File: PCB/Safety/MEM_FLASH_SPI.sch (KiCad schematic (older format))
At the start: 3 parts, among them U5 S70FL01GS

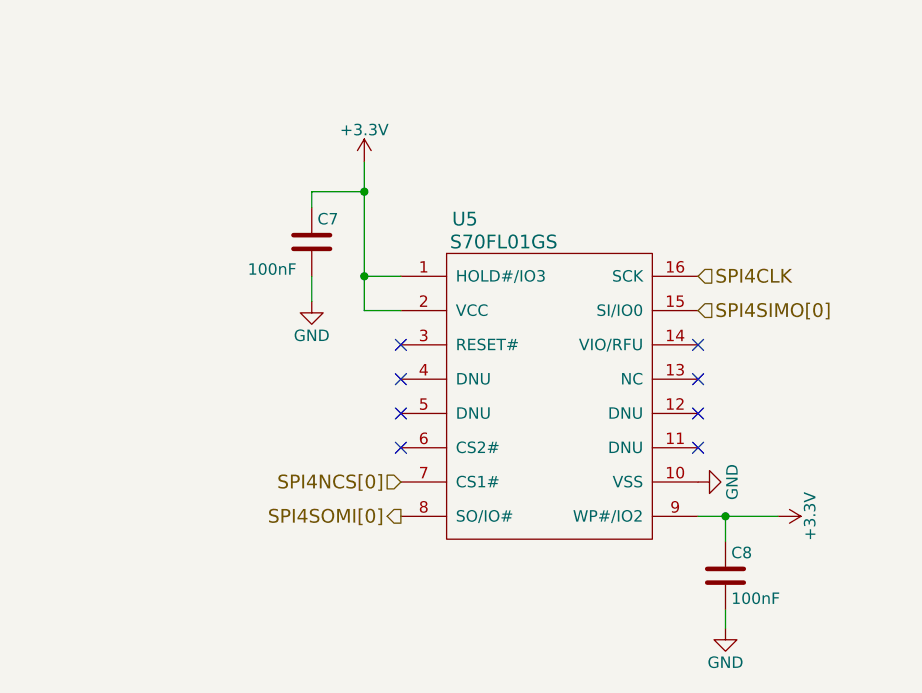
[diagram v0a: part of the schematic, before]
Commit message: New version (-4) from Fusari,s Drive.
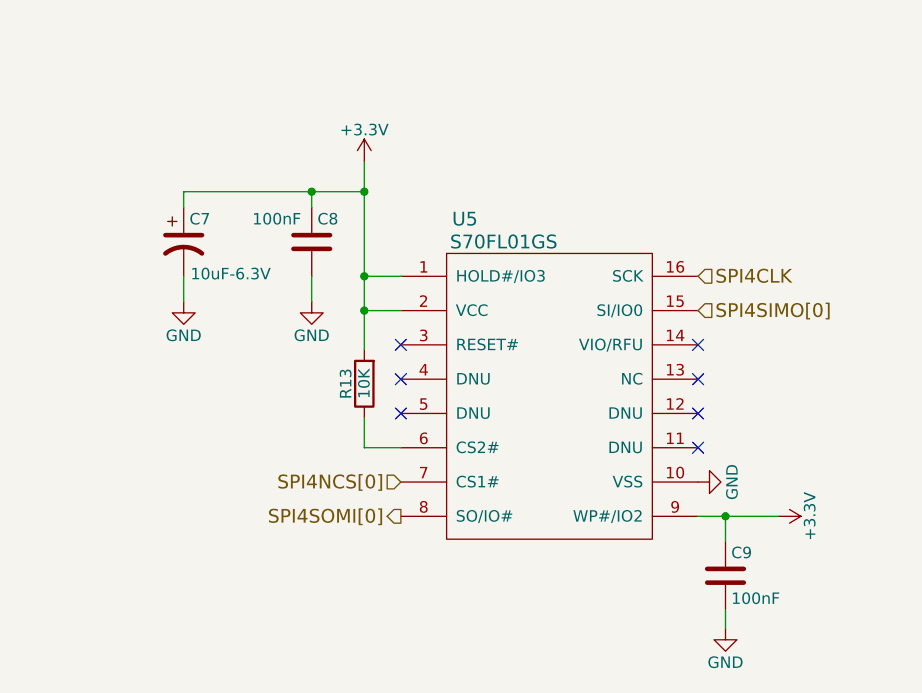
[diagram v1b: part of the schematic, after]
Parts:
- added C7: 10uF-6.3V, w_smd_cap:c_tant_A, symbol CP1
- added R13: 10K, w_smd_resistors:r_0603, symbol R
- C8: renamed from C7; Digikey (none) -> 478-5266-1-ND
- C9: renamed from C8; Digikey (none) -> 478-5266-1-ND
- U5: Digikey (none) -> 428-4016-1-ND
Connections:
- net +3V3: now also C7.1, R13.2
- net GND: now also C7.2
- net at U5.6 (CS2#): now also R13.1
- no-connect marks 8 -> 7
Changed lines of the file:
@@
 EESchema Schematic File Version 2
+LIBS:74xgxx
+LIBS:74xx
+LIBS:ac-dc
+LIBS:actel
+LIBS:adc-dac
+LIBS:Altera
+LIBS:analog_devices
+LIBS:analog_switches
+LIBS:atmel
+LIBS:audio
+LIBS:brooktre
+LIBS:cmos_ieee
+LIBS:cmos4000
+LIBS:conn
+LIBS:contrib
+LIBS:cypress
+LIBS:dc-dc
+LIBS:device
+LIBS:digital-audio
+LIBS:diode
+LIBS:display
+LIBS:dsp
+LIBS:elec-unifil
+LIBS:ESD_Protection
+LIBS:ftdi
+LIBS:gennum
+LIBS:graphic
+LIBS:hc11
+LIBS:intel
+LIBS:interface
+LIBS:ir
+LIBS:Lattice
+LIBS:linear
+LIBS:logo
+LIBS:maxim
+LIBS:memory
+LIBS:microchip
+LIBS:microchip_dspic33dsc
+LIBS:microchip_pic10mcu
+LIBS:microchip_pic12mcu
+LIBS:microchip_pic16mcu
+LIBS:microchip_pic18mcu
+LIBS:microchip_pic32mcu
+LIBS:microcontrollers
+LIBS:motor_drivers
+LIBS:motorola
+LIBS:msp430
+LIBS:nordicsemi
+LIBS:nxp_armmcu
+LIBS:onsemi
+LIBS:opto
+LIBS:Oscillators
+LIBS:philips
 LIBS:power
+LIBS:Power_Management
+LIBS:powerint
+LIBS:pspice
+LIBS:references
+LIBS:regul
+LIBS:relays
+LIBS:rfcom
+LIBS:sensors
+LIBS:silabs
+LIBS:siliconi
+LIBS:stm8
+LIBS:stm32
+LIBS:supertex
+LIBS:switches
+LIBS:texas
+LIBS:transf
+LIBS:transistors
+LIBS:ttl_ieee
+LIBS:valves
+LIBS:video
+LIBS:Xicor
+LIBS:xilinx
+LIBS:Zilog
 LIBS:CIAA_Safety_VTI_1.0-cache
 EELAYER 25 0
@@
 $Descr A4 11693 8268
 encoding utf-8
-Sheet 3 5
-Title "MEMORIA FLASH"
-Date "2016-06-02"
+Sheet 3 8
+Title "MODULO PROCESADOR SAFETY"
+Date "2016-09-01"
 Rev "1.0"
 Comp "PROYECTO CIAA SAFETY"
-Comment1 "Ing. Fusari Diego"
-Comment2 "MODULO PROCESADOR SAFETY"
-Comment3 "Licencia: Ver 'doc/LICENCIA.txt'"
+Comment1 "MEMORIA FLASH SPI"
+Comment2 "Revisión: Ferraro Matias"
+Comment3 "Autor: Ing. Fusari Diego Salvador"
 Comment4 ""
 $EndDescr
@@
 F 2 "w_smd_dil:soic-16" H 3490 5240 60  0001 C CNN
 F 3 "" H 3490 5240 60  0000 C CNN
+F 4 "428-4016-1-ND" H 3640 4390 60  0001 C CNN "Digikey"
 	1    3640 4390
 	1    0    0    -1
@@
 	2990 3890 2830 3890
 Wire Wire Line
-	2830 3390 2830 4040
+	2830 3390 2830 4210
 Wire Wire Line
 	2830 4040 2990 4040
 Connection ~ 2830 3890
 $Comp
-L C C7
+L C C8
 U 1 1 56C20E86
 P 2600 3740
-F 0 "C7" H 2625 3840 50  0000 L CNN
-F 1 "100nF" H 2320 3620 50  0000 L CNN
+F 0 "C8" H 2625 3840 50  0000 L CNN
+F 1 "100nF" H 2340 3840 50  0000 L CNN
 F 2 "w_smd_cap:c_0603" H 2638 3590 30  0001 C CNN
 F 3 "" H 2600 3740 60  0000 C CNN
+F 4 "478-5266-1-ND" H 2600 3740 60  0001 C CNN "Digikey"
 	1    2600 3740
 	1    0    0    -1
@@
 	2600 3590 2600 3520
 Wire Wire Line
-	2600 3520 2830 3520
+	2040 3520 2830 3520
 Connection ~ 2830 3520
 $Comp
-L +3.3V #PWR062
+L +3.3V #PWR013
 U 1 1 56C20F2E
 P 2830 3390
-F 0 "#PWR062" H 2830 3240 50  0001 C CNN
+F 0 "#PWR013" H 2830 3240 50  0001 C CNN
 F 1 "+3.3V" H 2830 3530 50  0000 C CNN
 F 2 "" H 2830 3390 60  0000 C CNN
@@
 $EndComp
 $Comp
-L GND #PWR063
+L GND #PWR014
 U 1 1 56C20F96
 P 2600 4000
-F 0 "#PWR063" H 2600 3750 50  0001 C CNN
+F 0 "#PWR014" H 2600 3750 50  0001 C CNN
 F 1 "GND" H 2600 3850 50  0000 C CNN
 F 2 "" H 2600 4000 60  0000 C CNN
@@
 	4290 4940 4640 4940
 $Comp
-L C C8
+L C C9
 U 1 1 56C210D1
 P 4410 5200
-F 0 "C8" H 4435 5300 50  0000 L CNN
+F 0 "C9" H 4435 5300 50  0000 L CNN
 F 1 "100nF" H 4435 5100 50  0000 L CNN
 F 2 "w_smd_cap:c_0603" H 4448 5050 30  0001 C CNN
 F 3 "" H 4410 5200 60  0000 C CNN
+F 4 "478-5266-1-ND" H 4410 5200 60  0001 C CNN "Digikey"
 	1    4410 5200
 	1    0    0    -1
@@
 Connection ~ 4410 4940
 $Comp
-L GND #PWR064
+L GND #PWR015
 U 1 1 56C211FB
 P 4410 5430
-F 0 "#PWR064" H 4410 5180 50  0001 C CNN
+F 0 "#PWR015" H 4410 5180 50  0001 C CNN
 F 1 "GND" H 4410 5280 50  0000 C CNN
 F 2 "" H 4410 5430 60  0000 C CNN
@@
 	4410 5430 4410 5350
 $Comp
-L +3.3V #PWR065
+L +3.3V #PWR016
 U 1 1 56C212DF
 P 4640 4940
-F 0 "#PWR065" H 4640 4790 50  0001 C CNN
+F 0 "#PWR016" H 4640 4790 50  0001 C CNN
 F 1 "+3.3V" H 4640 5080 50  0000 C CNN
 F 2 "" H 4640 4940 60  0000 C CNN
@@
 	0    1    1    0
 $EndComp
-NoConn ~ 2990 4640
-$Comp
-L GND #PWR066
+$Comp
+L GND #PWR017
 U 1 1 56C217DC
 P 4290 4790
-F 0 "#PWR066" H 4290 4540 50  0001 C CNN
+F 0 "#PWR017" H 4290 4540 50  0001 C CNN
 F 1 "GND" H 4290 4640 50  0000 C CNN
 F 2 "" H 4290 4790 60  0000 C CNN
@@
 Text Notes 5660 4640 0    99   ~ 0
 S25FL01GS - Memoria Flash no volatil de 1Gb (128 MB). \nContiene dos bloques de 512 Mb de los cuales se utiliza \nuno solo por lo que puede reemplazarse por \nS25FL512S (64MB).
+$Comp
+L CP1 C7
+U 1 1 57CA534A
+P 2040 3740
+F 0 "C7" H 2065 3840 50  0000 L CNN
+F 1 "10uF-6.3V" H 2070 3600 50  0000 L CNN
+F 2 "w_smd_cap:c_tant_A" H 2040 3740 60  0001 C CNN
+F 3 "" H 2040 3740 60  0000 C CNN
+F 4 "399-3685-1-ND" H 2040 3740 60  0001 C CNN "Digikey"
+	1    2040 3740
+	1    0    0    -1
+$EndComp
+Wire Wire Line
+	2040 3590 2040 3520
+Connection ~ 2600 3520
+$Comp
+L GND #PWR018
+U 1 1 57CA5512
+P 2040 4000
+F 0 "#PWR018" H 2040 3750 50  0001 C CNN
+F 1 "GND" H 2040 3850 50  0000 C CNN
+F 2 "" H 2040 4000 60  0000 C CNN
+F 3 "" H 2040 4000 60  0000 C CNN
+	1    2040 4000
+	1    0    0    -1
+$EndComp
+Wire Wire Line
+	2040 3890 2040 4000
+$Comp
+L R R13
+U 1 1 57C72411
+P 2830 4360
+F 0 "R13" V 2910 4360 50  0000 C CNN
+F 1 "10K" V 2830 4360 50  0000 C CNN
+F 2 "w_smd_resistors:r_0603" V 2760 4360 30  0001 C CNN
+F 3 "" H 2830 4360 30  0000 C CNN
+F 4 "311-10KGRCT-ND" H 2830 4360 60  0001 C CNN "Digikey"
+	1    2830 4360
+	-1   0    0    1
+$EndComp
+Wire Wire Line
+	2990 4640 2830 4640
+Wire Wire Line
+	2830 4640 2830 4510
+Connection ~ 2830 4040
 $EndSCHEMATC

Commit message: Added Diego Fusari's last version. Changes in texts, title blocks and sheet names.
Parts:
- C7: symbol CP1 -> CIAA_Safety_VTI_1.0-rescue:CP1
- C8, C9: symbol C -> CIAA_Safety_VTI_1.0-rescue:C
- R13: symbol R -> CIAA_Safety_VTI_1.0-rescue:R
- U5: symbol S70FL01GS -> CIAA_Safety_VTI_1.0-rescue:S70FL01GS
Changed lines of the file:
@@
-EESchema Schematic File Version 2
-LIBS:74xgxx
-LIBS:74xx
-LIBS:ac-dc
-LIBS:actel
-LIBS:adc-dac
-LIBS:Altera
-LIBS:analog_devices
-LIBS:analog_switches
-LIBS:atmel
-LIBS:audio
-LIBS:brooktre
-LIBS:cmos_ieee
-LIBS:cmos4000
-LIBS:conn
-LIBS:contrib
-LIBS:cypress
-LIBS:dc-dc
-LIBS:device
-LIBS:digital-audio
-LIBS:diode
-LIBS:display
-LIBS:dsp
-LIBS:elec-unifil
-LIBS:ESD_Protection
-LIBS:ftdi
-LIBS:gennum
-LIBS:graphic
-LIBS:hc11
-LIBS:intel
-LIBS:interface
-LIBS:ir
-LIBS:Lattice
-LIBS:linear
-LIBS:logo
-LIBS:maxim
-LIBS:memory
-LIBS:microchip
-LIBS:microchip_dspic33dsc
-LIBS:microchip_pic10mcu
-LIBS:microchip_pic12mcu
-LIBS:microchip_pic16mcu
-LIBS:microchip_pic18mcu
-LIBS:microchip_pic32mcu
-LIBS:microcontrollers
-LIBS:motor_drivers
-LIBS:motorola
-LIBS:msp430
-LIBS:nordicsemi
-LIBS:nxp_armmcu
-LIBS:onsemi
-LIBS:opto
-LIBS:Oscillators
-LIBS:philips
-LIBS:power
-LIBS:Power_Management
-LIBS:powerint
-LIBS:pspice
-LIBS:references
-LIBS:regul
-LIBS:relays
-LIBS:rfcom
-LIBS:sensors
-LIBS:silabs
-LIBS:siliconi
-LIBS:stm8
-LIBS:stm32
-LIBS:supertex
-LIBS:switches
-LIBS:texas
-LIBS:transf
-LIBS:transistors
-LIBS:ttl_ieee
-LIBS:valves
-LIBS:video
-LIBS:Xicor
-LIBS:xilinx
-LIBS:Zilog
+EESchema Schematic File Version 4
 LIBS:CIAA_Safety_VTI_1.0-cache
-EELAYER 25 0
+EELAYER 30 0
 EELAYER END
 $Descr A4 11693 8268
 encoding utf-8
 Sheet 3 8
-Title "MODULO PROCESADOR SAFETY"
+Title "MODULO PROCESADOR SAFETY-MEMORIA FLASH SPI"
 Date "2016-09-01"
 Rev "1.0"
@@
 SPI4SOMI[0]
 $Comp
-L S70FL01GS U5
+L CIAA_Safety_VTI_1.0-rescue:S70FL01GS U5
 U 1 1 56C20C2A
 P 3640 4390
@@
 	2990 3890 2830 3890
 Wire Wire Line
-	2830 3390 2830 4210
+	2830 3390 2830 3520
 Wire Wire Line
 	2830 4040 2990 4040
 Connection ~ 2830 3890
 $Comp
-L C C8
+L CIAA_Safety_VTI_1.0-rescue:C C8
 U 1 1 56C20E86
 P 2600 3740
@@
 	2600 3590 2600 3520
 Wire Wire Line
-	2040 3520 2830 3520
+	2040 3520 2600 3520
 Connection ~ 2830 3520
 $Comp
-L +3.3V #PWR013
+L power:+3.3V #PWR013
 U 1 1 56C20F2E
 P 2830 3390
@@
 $EndComp
 $Comp
-L GND #PWR014
+L power:GND #PWR014
 U 1 1 56C20F96
 P 2600 4000
@@
 	2600 3890 2600 4000
 Wire Wire Line
-	4290 4940 4640 4940
-$Comp
-L C C9
+	4290 4940 4410 4940
+$Comp
+L CIAA_Safety_VTI_1.0-rescue:C C9
 U 1 1 56C210D1
 P 4410 5200
@@
 Connection ~ 4410 4940
 $Comp
-L GND #PWR015
+L power:GND #PWR015
 U 1 1 56C211FB
 P 4410 5430
@@
 	4410 5430 4410 5350
 $Comp
-L +3.3V #PWR016
+L power:+3.3V #PWR016
 U 1 1 56C212DF
 P 4640 4940
@@
 $EndComp
 $Comp
-L GND #PWR017
+L power:GND #PWR017
 U 1 1 56C217DC
 P 4290 4790
@@
 S25FL01GS - Memoria Flash no volatil de 1Gb (128 MB). \nContiene dos bloques de 512 Mb de los cuales se utiliza \nuno solo por lo que puede reemplazarse por \nS25FL512S (64MB).
 $Comp
-L CP1 C7
+L CIAA_Safety_VTI_1.0-rescue:CP1 C7
 U 1 1 57CA534A
 P 2040 3740
@@
 Connection ~ 2600 3520
 $Comp
-L GND #PWR018
+L power:GND #PWR018
 U 1 1 57CA5512
 P 2040 4000
@@
 	2040 3890 2040 4000
 $Comp
-L R R13
+L CIAA_Safety_VTI_1.0-rescue:R R13
 U 1 1 57C72411
 P 2830 4360
@@
 	2830 4640 2830 4510
 Connection ~ 2830 4040
+Wire Wire Line
+	2830 3890 2830 4040
+Wire Wire Line
+	2830 3520 2830 3890
+Wire Wire Line
+	4410 4940 4640 4940
+Wire Wire Line
+	2600 3520 2830 3520
+Wire Wire Line
+	2830 4040 2830 4210
 $EndSCHEMATC
